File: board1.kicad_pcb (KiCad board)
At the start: 2 copper layers, 101.2 x 101.2 mm, 24 parts, among them J6 XT30 Male Connector, U1 BNO085, U2 Teensy_4.0, U3 Raspberry_PI_Zero_W, U4 D24V50F5

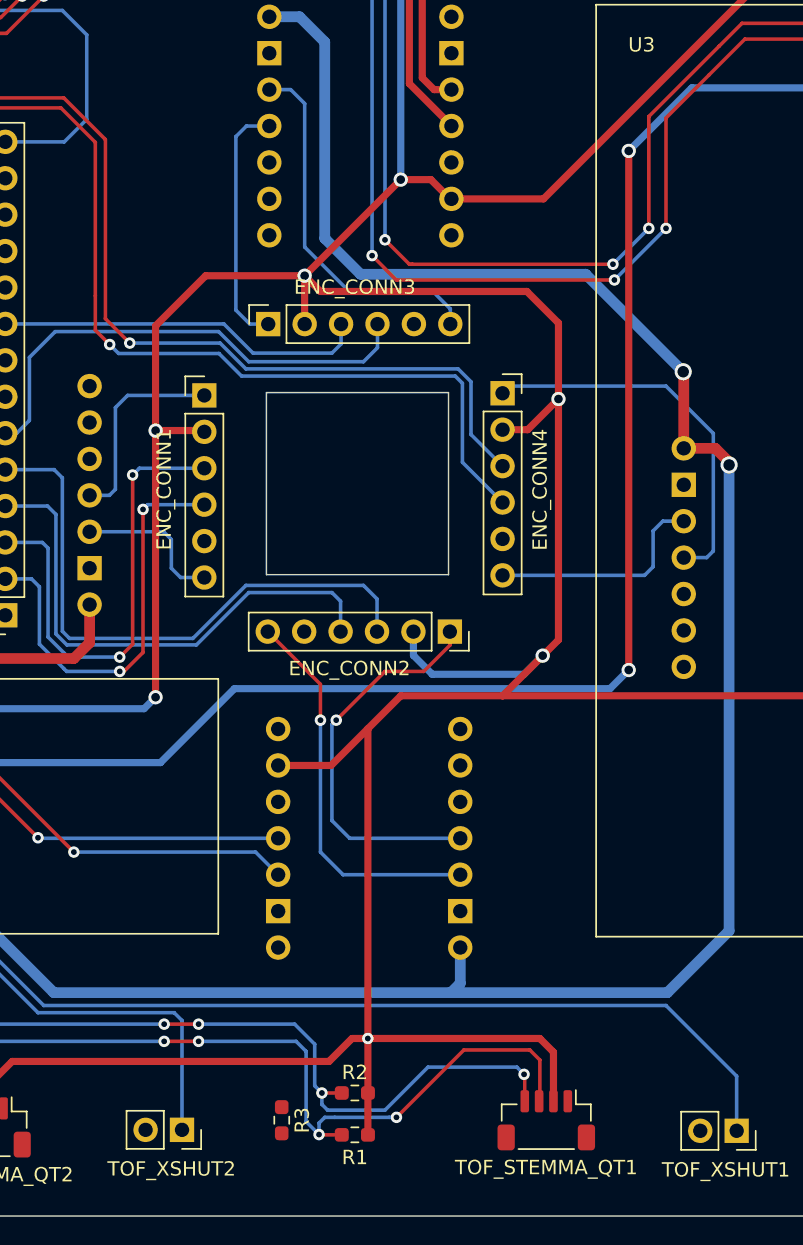
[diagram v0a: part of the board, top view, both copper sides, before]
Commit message: Updated PCB
Flipped Encoder, Increased Trace Size, and Changed Resistors to be 0805
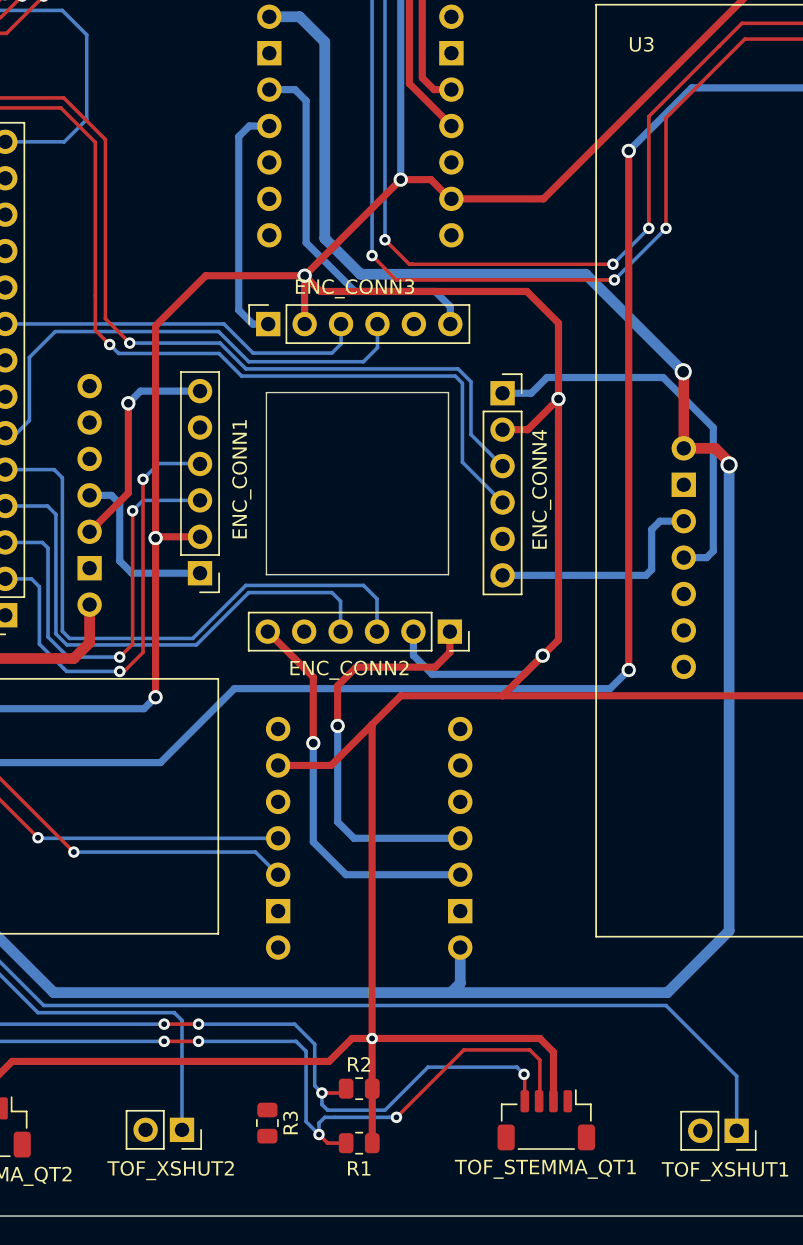
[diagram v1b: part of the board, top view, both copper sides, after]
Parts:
- R1, R2, R3: footprint board1_footprints:Resistor -> Resistor_SMD:R_0805_2012Metric
- moved ENC_CONN1 12.4 mm to (140.2, 114.3), turned to 180 degrees
- moved R3 1.02 mm to (144.9, 152.7)
- moved R1 0.65 mm to (151.3, 154.1)
- moved R2 0.42 mm to (151.3, 150.3)
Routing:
- net /MOTOR_1_PIN1: track 10.5 -> 15.4 mm, vias 0 -> 1
- net /ENC_1_PINB: track 33.2 -> 30.5 mm
- net /ENC_1_PINA: track 29.6 -> 31.7 mm
- net /MOTOR_1_PIN2: track 14.2 -> 12.3 mm
- net /MOTOR_2_PIN2: track 27.6 -> 28.8 mm
- net /MOTOR_3_PIN2: track 18.0 -> 17.0 mm
- net /MOTOR_4_PIN2: track 26.7 -> 27.5 mm
- net /SDA_LINE: track 235.9 -> 236.4 mm

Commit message: Added suggestion for 4 layer board
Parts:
- moved R3 93.7 mm to (60.0, 113.0)
- moved ENC_CONN3 47.2 mm to (98.7, 87.6)
- moved ENC_CONN4 47.2 mm to (115.0, 92.4)
- moved MC1 47.2 mm to (79.8, 113.0)
- moved R1 47.2 mm to (105.0, 144.7)
- moved R2 47.2 mm to (105.0, 140.9)
- moved TOF_STEMMA_QT3 47.2 mm to (134.7, 54.6)
- moved TOF_XSHUT1 47.2 mm to (131.3, 143.8)
- moved ENC_CONN2 47.2 mm to (111.3, 109.0)
- moved J6 47.2 mm to (61.7, 120.8)
- moved MC2 47.2 mm to (105.7, 136.9)
- moved TOF_STEMMA_QT1 47.2 mm to (118.0, 143.1)
- moved TOF_STEMMA_QT2 47.2 mm to (78.7, 143.6)
- moved TOF_STEMMA_QT4 47.2 mm to (83.7, 55.6)
- moved TOF_XSHUT2 47.2 mm to (92.6, 143.8)
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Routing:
- net GNDREF: track 0.00 -> 2.09 mm, vias 0 -> 46
- net /BATTERY_GROUND: track 0.00 -> 2.09 mm, vias 0 -> 1
- added copper zone on In2.Cu, net /12V
- added copper zone on In1.Cu, net /BATTERY_GROUND
- added copper zone on B.Cu, net GNDREF
- added copper zone on F.Cu, net GNDREF
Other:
- copper layers 2 -> 4
- board text removed: "circles are arbitrary radius, can be resized for mounting holes later do not edit for now, if need be, just change radius"
